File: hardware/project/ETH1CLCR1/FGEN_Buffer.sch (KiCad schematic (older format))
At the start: 62 parts, among them K701 9012, K702 9012, K703 9012, K704 9012, Q701 BC847W, Q702 BC847W, Q703 BC847W, Q704 BC847W, Q705 MMBT4401L, Q706 MMBT4403L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

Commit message: PCB done.
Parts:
- added C717: 10u, Capacitor_SMD:C_1206_3216Metric_Pad1.42x1.75mm_HandSolder, symbol Device:C
- added R724: 0, Resistor_SMD:R_0603_1608Metric_Pad1.05x0.95mm_HandSolder, symbol Device:R
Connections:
- net HCUR: no longer R721.2, U702.2 (-)
- net at C708.2, K701.1, K702.1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: now also C717.2, R724.2
- new net: C717.1, R721.2, R724.1, U702.2 (-)
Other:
- moved on the sheet: C701, C702, C703, C704, C708, C713, C715, C716, D701, D702, D703, D704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

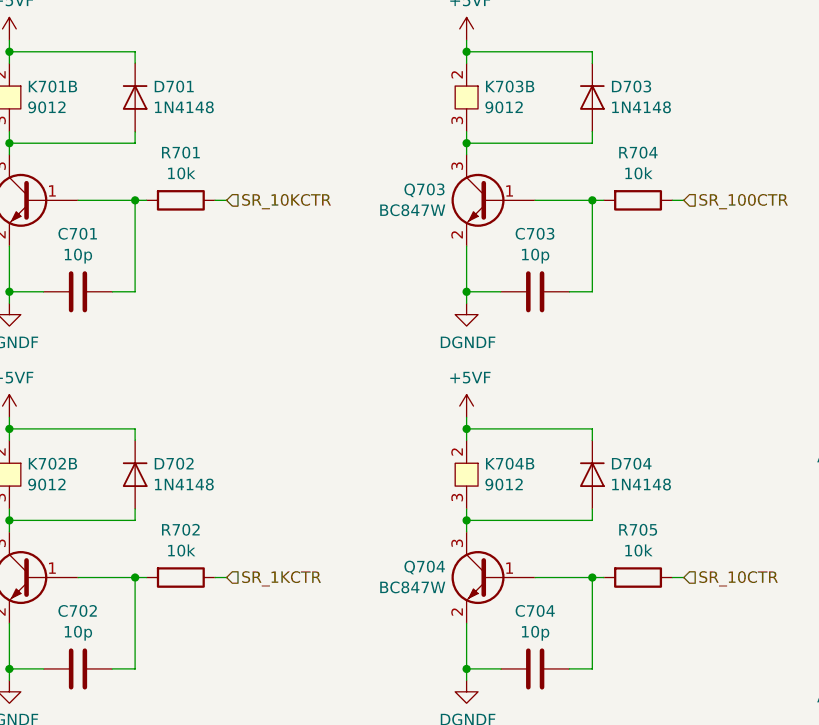
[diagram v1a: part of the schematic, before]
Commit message: Range BC847 base serial resistors value from 10k to 1k.
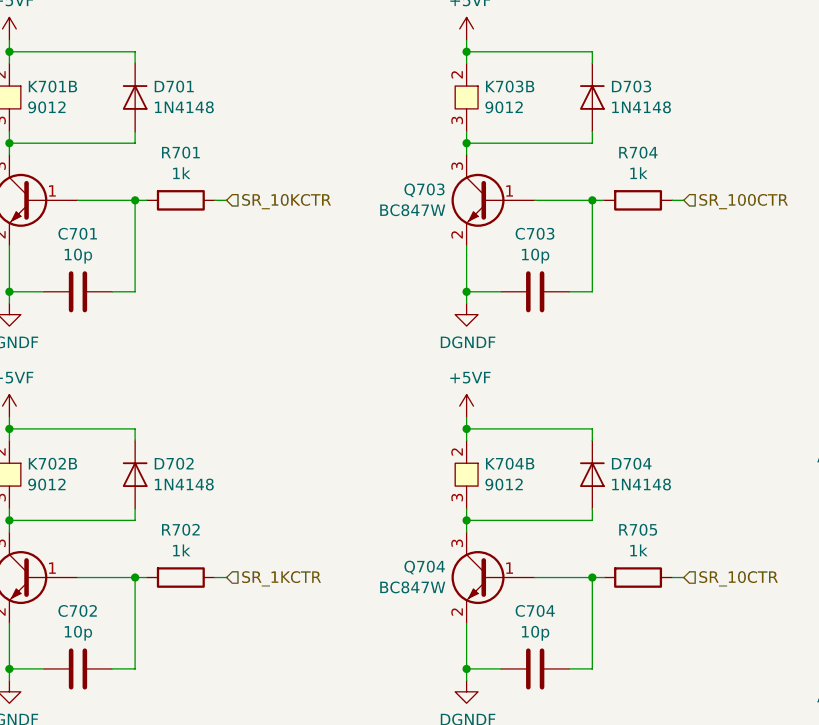
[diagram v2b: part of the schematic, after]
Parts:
- R701, R702, R704, R705: value 10k -> 1k
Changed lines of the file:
@@
 P 1700 5450
 F 0 "R701" V 1493 5450 50  0000 C CNN
-F 1 "10k" V 1584 5450 50  0000 C CNN
+F 1 "1k" V 1584 5450 50  0000 C CNN
 F 2 "Resistor_SMD:R_0603_1608Metric_Pad1.05x0.95mm_HandSolder" V 1630 5450 50  0001 C CNN
 F 3 "~" H 1700 5450 50  0001 C CNN
@@
 P 1700 7100
 F 0 "R702" V 1493 7100 50  0000 C CNN
-F 1 "10k" V 1584 7100 50  0000 C CNN
+F 1 "1k" V 1584 7100 50  0000 C CNN
 F 2 "Resistor_SMD:R_0603_1608Metric_Pad1.05x0.95mm_HandSolder" V 1630 7100 50  0001 C CNN
 F 3 "~" H 1700 7100 50  0001 C CNN
@@
 P 3700 5450
 F 0 "R704" V 3493 5450 50  0000 C CNN
-F 1 "10k" V 3584 5450 50  0000 C CNN
+F 1 "1k" V 3584 5450 50  0000 C CNN
 F 2 "Resistor_SMD:R_0603_1608Metric_Pad1.05x0.95mm_HandSolder" V 3630 5450 50  0001 C CNN
 F 3 "~" H 3700 5450 50  0001 C CNN
@@
 P 3700 7100
 F 0 "R705" V 3493 7100 50  0000 C CNN
-F 1 "10k" V 3584 7100 50  0000 C CNN
+F 1 "1k" V 3584 7100 50  0000 C CNN
 F 2 "Resistor_SMD:R_0603_1608Metric_Pad1.05x0.95mm_HandSolder" V 3630 7100 50  0001 C CNN
 F 3 "~" H 3700 7100 50  0001 C CNN

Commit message: Changed BC847W base resistor from 1k to 10k.
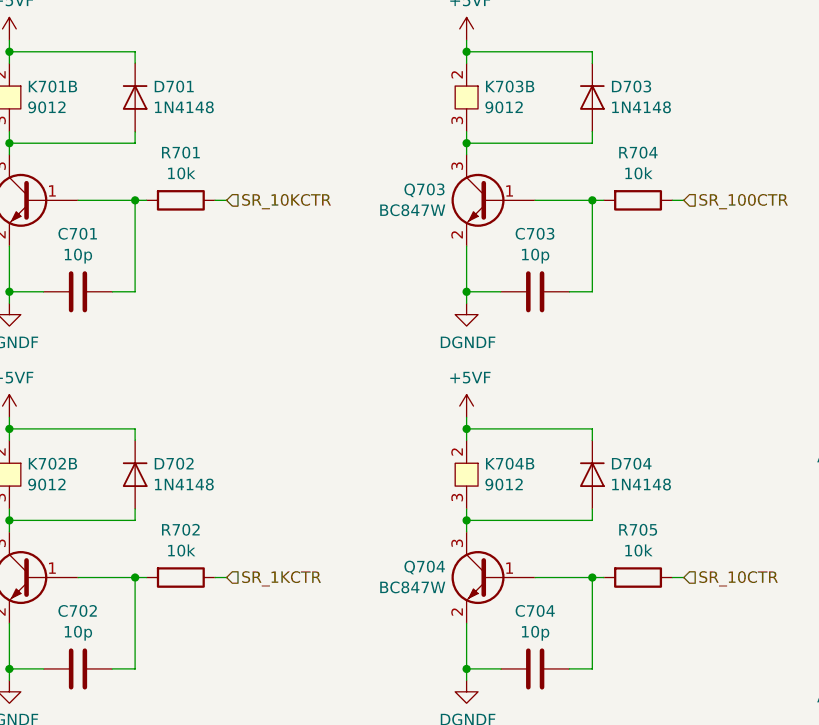
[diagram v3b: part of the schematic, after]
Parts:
- R701, R702, R704, R705: value 1k -> 10k
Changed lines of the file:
@@
 P 1700 5450
 F 0 "R701" V 1493 5450 50  0000 C CNN
-F 1 "1k" V 1584 5450 50  0000 C CNN
+F 1 "10k" V 1584 5450 50  0000 C CNN
 F 2 "Resistor_SMD:R_0603_1608Metric_Pad1.05x0.95mm_HandSolder" V 1630 5450 50  0001 C CNN
 F 3 "~" H 1700 5450 50  0001 C CNN
@@
 P 1700 7100
 F 0 "R702" V 1493 7100 50  0000 C CNN
-F 1 "1k" V 1584 7100 50  0000 C CNN
+F 1 "10k" V 1584 7100 50  0000 C CNN
 F 2 "Resistor_SMD:R_0603_1608Metric_Pad1.05x0.95mm_HandSolder" V 1630 7100 50  0001 C CNN
 F 3 "~" H 1700 7100 50  0001 C CNN
@@
 P 3700 5450
 F 0 "R704" V 3493 5450 50  0000 C CNN
-F 1 "1k" V 3584 5450 50  0000 C CNN
+F 1 "10k" V 3584 5450 50  0000 C CNN
 F 2 "Resistor_SMD:R_0603_1608Metric_Pad1.05x0.95mm_HandSolder" V 3630 5450 50  0001 C CNN
 F 3 "~" H 3700 5450 50  0001 C CNN
@@
 P 3700 7100
 F 0 "R705" V 3493 7100 50  0000 C CNN
-F 1 "1k" V 3584 7100 50  0000 C CNN
+F 1 "10k" V 3584 7100 50  0000 C CNN
 F 2 "Resistor_SMD:R_0603_1608Metric_Pad1.05x0.95mm_HandSolder" V 3630 7100 50  0001 C CNN
 F 3 "~" H 3700 7100 50  0001 C CNN

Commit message: Small changes in schematics and PCB
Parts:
- R712: value 330 -> 680
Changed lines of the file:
@@
 P 6500 3950
 F 0 "R712" V 6293 3950 50  0000 C CNN
-F 1 "330" V 6384 3950 50  0000 C CNN
+F 1 "680" V 6384 3950 50  0000 C CNN
 F 2 "Resistor_SMD:R_0603_1608Metric_Pad1.05x0.95mm_HandSolder" V 6430 3950 50  0001 C CNN
 F 3 "~" H 6500 3950 50  0001 C CNN

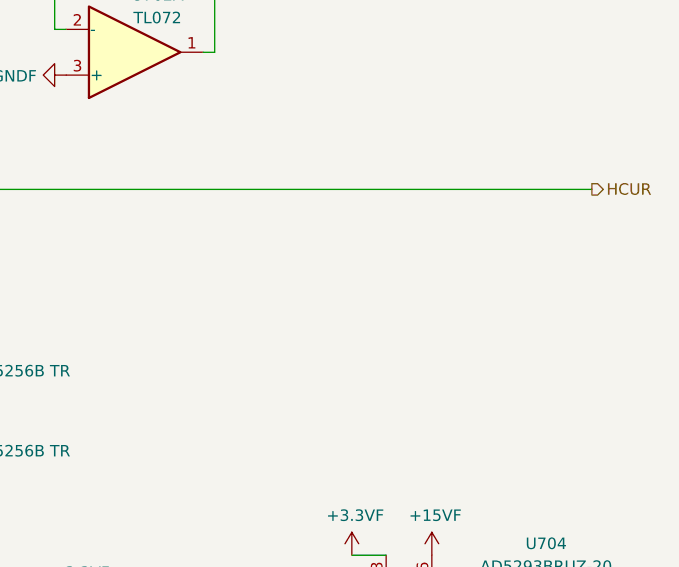
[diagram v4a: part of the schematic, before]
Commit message: Was able to set the SPI3 (MCU2) to run with 80 MHZ clock speed with AD7380. Using HAL lib for SPI and GPIO, too slow switching. Need to change to LL with DMA.
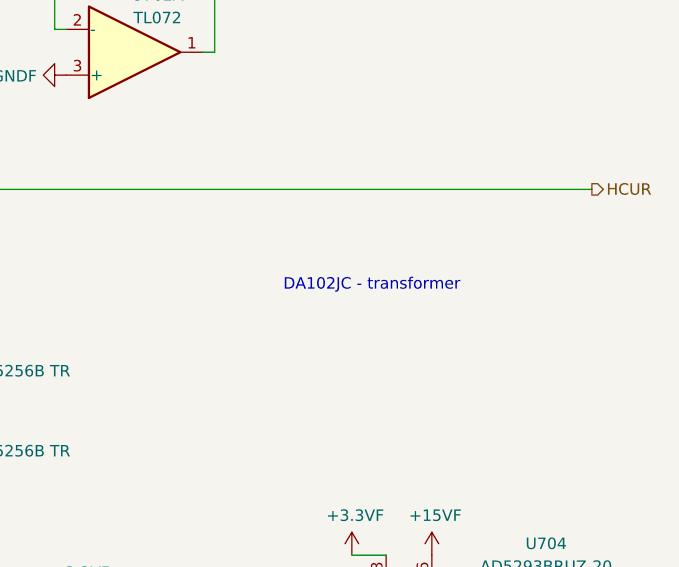
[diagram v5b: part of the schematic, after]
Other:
- note added: "DA102JC - transformer"
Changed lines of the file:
@@
 Wire Wire Line
 	7900 1300 7900 900
+Text Notes 8900 3800 0    50   ~ 0
+DA102JC - transformer
 $EndSCHEMATC
